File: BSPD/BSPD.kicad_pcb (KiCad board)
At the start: 2 copper layers, 160 x 124.7 mm, 30 parts, among them J1 DT13-48PABCD-R015, U1 LM317_TO-252, U10 DK1A1B-12V, U2 OP AMP, U3 OP AMP, U4 Inverter (Not Gate), U5 2x4 OR GATE, U6 LM555N, U7 NSL-32, U9 AND GATE

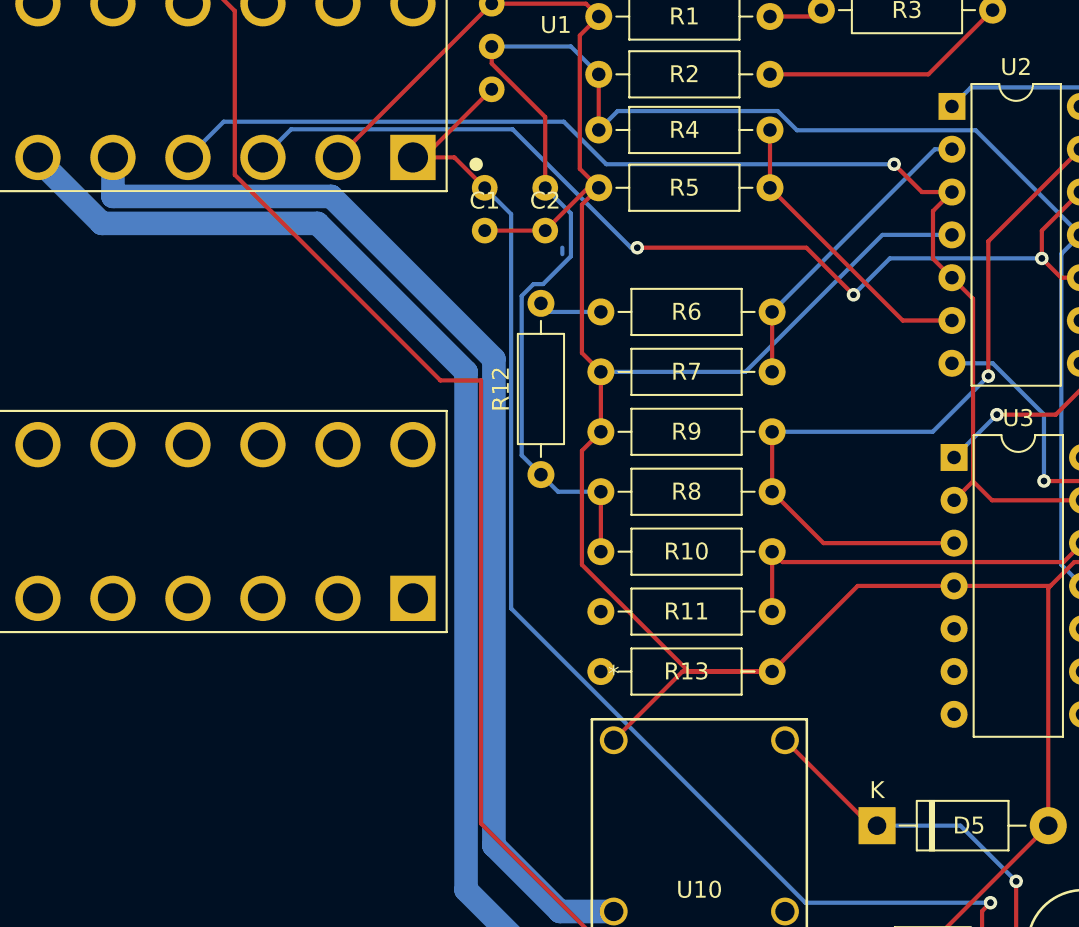
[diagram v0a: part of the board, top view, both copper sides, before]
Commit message: Updated timer and connections
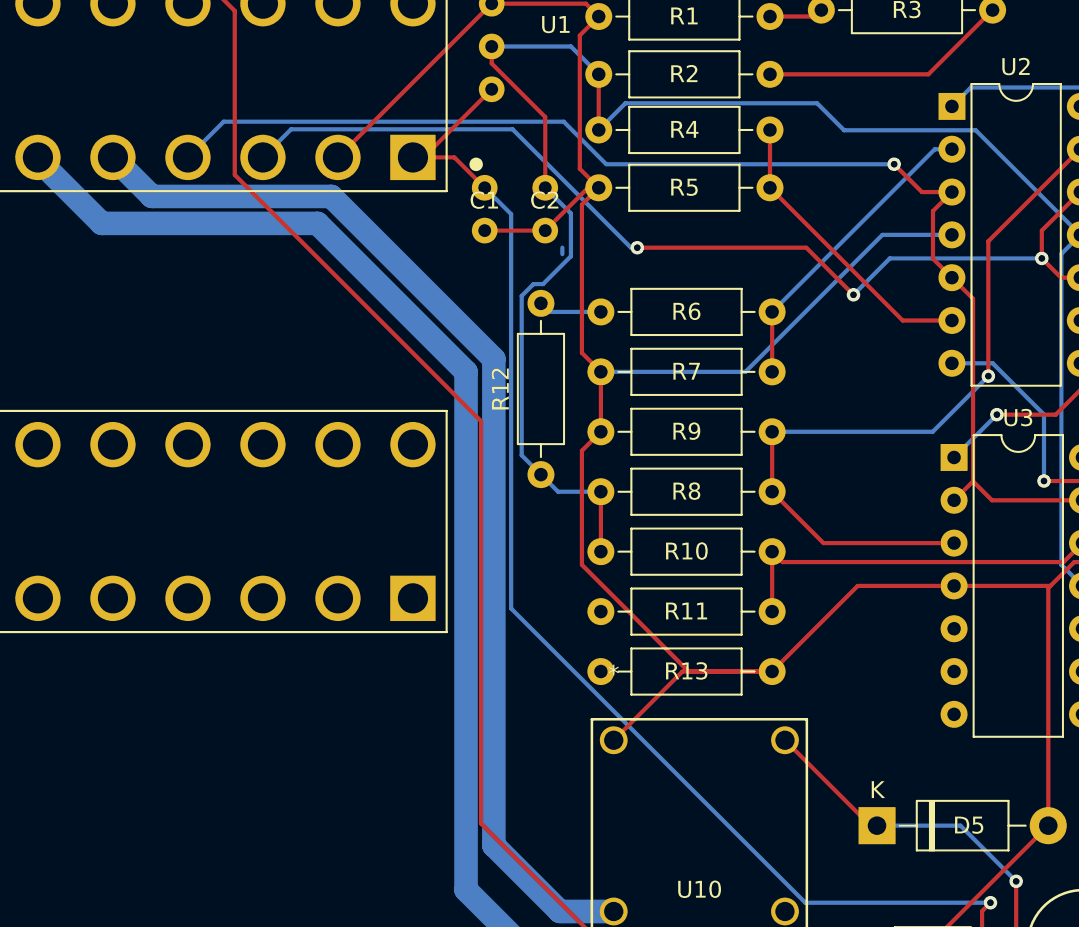
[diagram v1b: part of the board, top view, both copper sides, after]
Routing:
- net /BSPD Fault: track 109.3 -> 107.9 mm
- net /Shutdown In: track 66.5 -> 65.2 mm
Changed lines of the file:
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@@
   (via (at 102.39986 74.395662) (size 0.8) (drill 0.4) (layers "F.Cu" "B.Cu") (net 2))
   (via (at 101.201 47.451802) (size 0.8) (drill 0.4) (layers "F.Cu" "B.Cu") (net 2))
+  (segment (start 92.964 48.703802) (end 86.759 42.498802) (width 0.25) (layer "B.Cu") (net 2))
   (segment (start 62.738 49.975198) (end 61.088396 51.624802) (width 0.25) (layer "B.Cu") (net 2))
   (segment (start 62.738 47.433802) (end 62.738 49.975198) (width 0.25) (layer "B.Cu") (net 2))
-  (segment (start 86.759 42.498802) (end 76.150878 42.498802) (width 0.25) (layer "B.Cu") (net 2))
   (segment (start 91.839 49.828802) (end 92.964 48.703802) (width 0.25) (layer "B.Cu") (net 2))
   (segment (start 61.214 45.909802) (end 62.738 47.433802) (width 0.25) (layer "B.Cu") (net 2))
   (segment (start 58.039 37.527802) (end 62.738 37.527802) (width 0.25) (layer "B.Cu") (net 2))
-  (segment (start 76.150878 42.498802) (end 75.007878 41.355802) (width 0.25) (layer "B.Cu") (net 2))
   (segment (start 94.216 47.451802) (end 92.964 48.703802) (width 0.25) (layer "B.Cu") (net 2))
-  (segment (start 75.007878 41.355802) (end 65.514 41.355802) (width 0.25) (layer "B.Cu") (net 2))
   (segment (start 59.817 52.326924) (end 59.817 61.784802) (width 0.25) (layer "B.Cu") (net 2))
   (segment (start 91.839 68.279802) (end 91.839 49.828802) (width 0.25) (layer "B.Cu") (net 2))
   (segment (start 101.201 47.451802) (end 94.216 47.451802) (width 0.25) (layer "B.Cu") (net 2))
-  (segment (start 65.514 41.355802) (end 64.389 42.480802) (width 0.25) (layer "B.Cu") (net 2))
   (segment (start 107.696 40.956802) (end 101.201 47.451802) (width 0.25) (layer "B.Cu") (net 2))
+  (segment (start 65.975802 40.894) (end 64.389 42.480802) (width 0.25) (layer "B.Cu") (net 2))
+  (segment (start 78.947802 42.498802) (end 77.343 40.894) (width 0.25) (layer "B.Cu") (net 2))
   (segment (start 59.817 61.784802) (end 60.96 62.927802) (width 0.25) (layer "B.Cu") (net 2))
   (segment (start 102.27286 74.395662) (end 100.076 72.198802) (width 0.25) (layer "B.Cu") (net 2))
   (segment (start 62.738 37.527802) (end 64.389 39.178802) (width 0.25) (layer "B.Cu") (net 2))
   (segment (start 61.976 63.943802) (end 60.96 62.927802) (width 0.25) (layer "B.Cu") (net 2))
-  (segment (start 92.964 48.703802) (end 86.759 42.498802) (width 0.25) (layer "B.Cu") (net 2))
   (segment (start 64.516 63.943802) (end 61.976 63.943802) (width 0.25) (layer "B.Cu") (net 2))
   (segment (start 60.519122 51.624802) (end 59.817 52.326924) (width 0.25) (layer "B.Cu") (net 2))
+  (segment (start 77.343 40.894) (end 65.975802 40.894) (width 0.25) (layer "B.Cu") (net 2))
+  (segment (start 86.759 42.498802) (end 78.947802 42.498802) (width 0.25) (layer "B.Cu") (net 2))
   (segment (start 93.091 69.531802) (end 91.839 68.279802) (width 0.25) (layer "B.Cu") (net 2))
   (segment (start 61.088396 51.624802) (end 60.519122 51.624802) (width 0.25) (layer "B.Cu") (net 2))
@@
   (segment (start 100.076 51.116802) (end 100.076 51.916802) (width 0.25) (layer "F.Cu") (net 50))
   (segment (start 93.091 58.901802) (end 93.091 61.911802) (width 0.25) (layer "F.Cu") (net 50))
+  (segment (start 35.565 44.109802) (end 37.878 46.422802) (width 1.4) (layer "B.Cu") (net 51))
   (segment (start 58.166 84.930802) (end 62.0837 88.848502) (width 1.4) (layer "B.Cu") (net 51))
-  (segment (start 35.565 44.109802) (end 35.565 46.422802) (width 1.4) (layer "B.Cu") (net 51))
-  (segment (start 48.519 46.422802) (end 58.166 56.069802) (width 1.4) (layer "B.Cu") (net 51))
+  (segment (start 37.878 46.422802) (end 48.519 46.422802) (width 1.4) (layer "B.Cu") (net 51))
   (segment (start 58.166 56.069802) (end 58.166 84.930802) (width 1.4) (layer "B.Cu") (net 51))
   (segment (start 62.0837 88.848502) (end 65.278 88.848502) (width 1.4) (layer "B.Cu") (net 51))
-  (segment (start 35.565 46.422802) (end 48.519 46.422802) (width 1.4) (layer "B.Cu") (net 51))
+  (segment (start 48.519 46.422802) (end 58.166 56.069802) (width 1.4) (layer "B.Cu") (net 51))
   (segment (start 56.515 56.831802) (end 56.515 87.565802) (width 1.4) (layer "B.Cu") (net 52))
   (segment (start 31.115 44.109802) (end 31.115 44.235544) (width 1.4) (layer "B.Cu") (net 52))
@@
   (segment (start 47.706 48.022802) (end 56.515 56.831802) (width 1.4) (layer "B.Cu") (net 52))
   (segment (start 34.902258 48.022802) (end 47.706 48.022802) (width 1.4) (layer "B.Cu") (net 52))
-  (segment (start 57.404 83.628802) (end 57.404 57.339802) (width 0.25) (layer "F.Cu") (net 53))
   (segment (start 32.785 33.319802) (end 31.115 34.989802) (width 0.25) (layer "F.Cu") (net 53))
+  (segment (start 57.404 83.628802) (end 57.404 59.752802) (width 0.25) (layer "F.Cu") (net 53))
+  (segment (start 42.795 35.415302) (end 40.6995 33.319802) (width 0.25) (layer "F.Cu") (net 53))
+  (segment (start 42.795 45.143802) (end 42.795 35.415302) (width 0.25) (layer "F.Cu") (net 53))
+  (segment (start 57.404 59.752802) (end 42.795 45.143802) (width 0.25) (layer "F.Cu") (net 53))
+  (segment (start 79.248 105.472802) (end 57.404 83.628802) (width 0.25) (layer "F.Cu") (net 53))
   (segment (start 40.6995 33.319802) (end 32.785 33.319802) (width 0.25) (layer "F.Cu") (net 53))
-  (segment (start 79.248 105.472802) (end 57.404 83.628802) (width 0.25) (layer "F.Cu") (net 53))
-  (segment (start 42.795 45.143802) (end 42.795 35.415302) (width 0.25) (layer "F.Cu") (net 53))
-  (segment (start 42.795 35.415302) (end 40.6995 33.319802) (width 0.25) (layer "F.Cu") (net 53))
-  (segment (start 54.991 57.339802) (end 42.795 45.143802) (width 0.25) (layer "F.Cu") (net 53))
-  (segment (start 57.404 57.339802) (end 54.991 57.339802) (width 0.25) (layer "F.Cu") (net 53))
   (segment (start 82.794 101.926802) (end 79.248 105.472802) (width 0.25) (layer "B.Cu") (net 53))
   (segment (start 87.259 101.926802) (end 82.794 101.926802) (width 0.25) (layer "B.Cu") (net 53))
